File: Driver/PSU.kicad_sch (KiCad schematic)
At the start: 29 parts, among them J5 Jack-DC, U1 LM2596S-ADJ, U2 LM2674M-5.0, U3 LD1117S33TR

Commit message: 2
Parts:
- L2: footprint SamacSys_Parts:LQH43MN470K03L -> Inductor_SMD:L_1812_4532Metric_Pad1.30x3.40mm_HandSolder
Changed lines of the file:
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@@
 			)
 		)
-		(property "Footprint" "SamacSys_Parts:LQH43MN470K03L"
+		(property "Footprint" "Inductor_SMD:L_1812_4532Metric_Pad1.30x3.40mm_HandSolder"
 			(at 243.84 64.77 0)
 			(effects

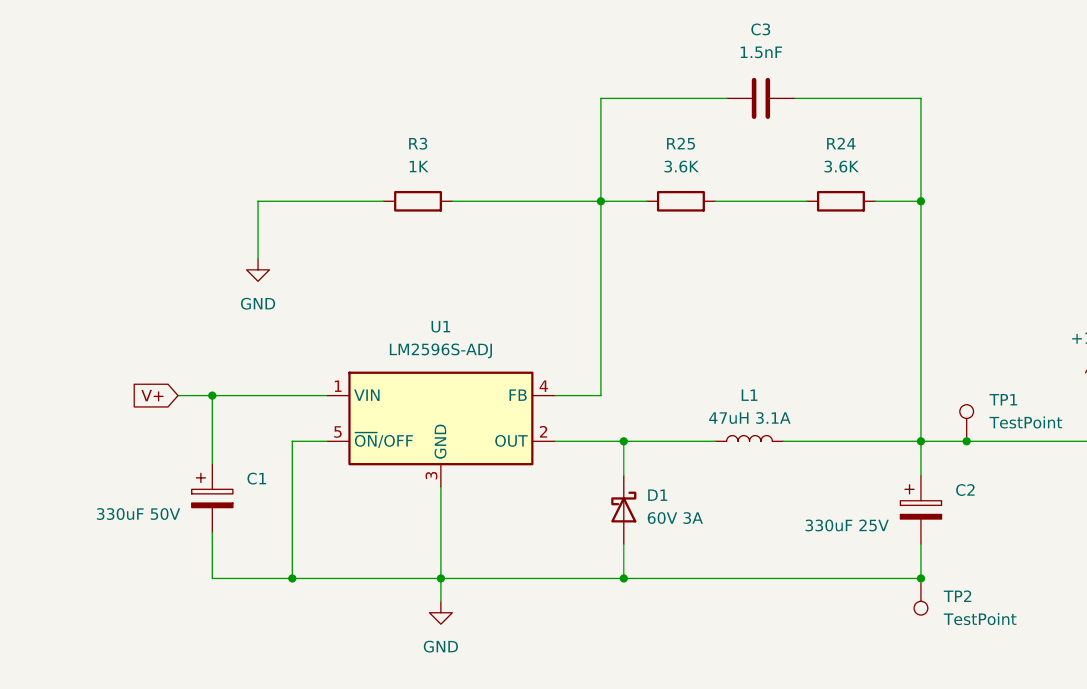
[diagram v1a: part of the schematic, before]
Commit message: Update a Connector and Trimpot
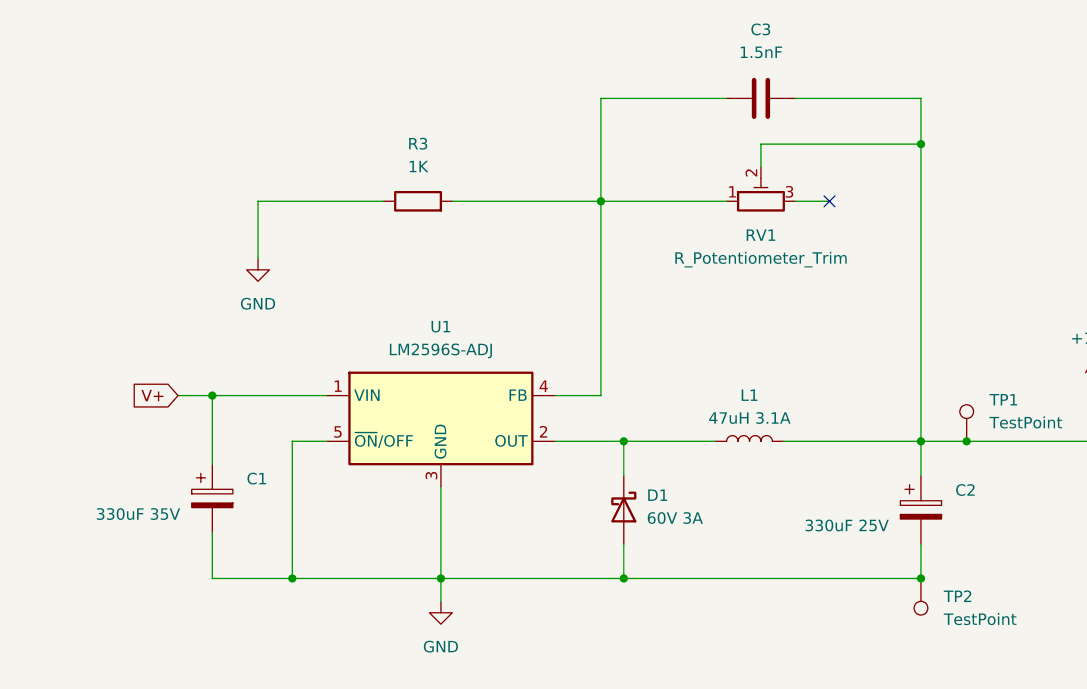
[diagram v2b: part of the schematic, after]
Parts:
- removed R24, R25: 3.6K, LED_SMD:LED_0805_2012Metric_Pad1.15x1.40mm_HandSolder, symbol Device:R
- added RV1: R_Potentiometer_Trim, Potentiometer_THT:Potentiometer_Bourns_3296W_Vertical, symbol Device:R_Potentiometer_Trim
- C1: value 330uF 50V -> 330uF 35V
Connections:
- net +10V: now also RV1.2
- net at C3.1, R3.2, U1.4 (FB): now also RV1.1
- no-connect marks 3 -> 4
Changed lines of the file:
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@@
-	)
-	(junction
-		(at 116.84 33.02)
-		(diameter 0)
-		(color 0 0 0 0)
 	)
 	(junction
@@
 	)
 	(junction
+		(at 116.84 26.67)
+		(diameter 0)
+		(color 0 0 0 0)
+	)
+	(junction
 		(at 241.3 54.61)
 		(diameter 0)
@@
 	)
 	(no_connect
+		(at 106.68 33.02)
+	)
+	(no_connect
 		(at 191.77 59.69)
 	)
@@
 	(wire
 		(pts
-			(xy 93.98 33.02) (xy 104.14 33.02)
-		)
-		(stroke
-			(width 0)
-			(type default)
-		)
-	)
-	(wire
-		(pts
 			(xy 38.1 74.93) (xy 46.99 74.93)
 		)
@@
 	(wire
 		(pts
-			(xy 81.28 33.02) (xy 86.36 33.02)
+			(xy 81.28 33.02) (xy 95.25 33.02)
 		)
 		(stroke
@@
 	(wire
 		(pts
+			(xy 102.87 33.02) (xy 106.68 33.02)
+		)
+		(stroke
+			(width 0)
+			(type default)
+		)
+	)
+	(wire
+		(pts
 			(xy 162.56 71.12) (xy 162.56 78.74)
 		)
@@
 	(wire
 		(pts
-			(xy 111.76 33.02) (xy 116.84 33.02)
-		)
-		(stroke
-			(width 0)
-			(type default)
-		)
-	)
-	(wire
-		(pts
 			(xy 201.93 119.38) (xy 214.63 119.38)
 		)
@@
 	(wire
 		(pts
-			(xy 116.84 21.59) (xy 116.84 33.02)
+			(xy 116.84 21.59) (xy 116.84 26.67)
 		)
 		(stroke
@@
 	(wire
 		(pts
-			(xy 116.84 33.02) (xy 116.84 59.69)
-		)
-		(stroke
-			(width 0)
-			(type default)
-		)
-	)
-	(wire
-		(pts
 			(xy 83.82 71.12) (xy 83.82 74.93)
 		)
@@
 	(wire
 		(pts
+			(xy 116.84 26.67) (xy 116.84 59.69)
+		)
+		(stroke
+			(width 0)
+			(type default)
+		)
+	)
+	(wire
+		(pts
 			(xy 172.72 119.38) (xy 172.72 123.19)
 		)
@@
 	(wire
 		(pts
+			(xy 99.06 26.67) (xy 116.84 26.67)
+		)
+		(stroke
+			(width 0)
+			(type default)
+		)
+	)
+	(wire
+		(pts
 			(xy 204.47 80.01) (xy 204.47 78.74)
 		)
@@
 		(pts
 			(xy 64.77 33.02) (xy 81.28 33.02)
+		)
+		(stroke
+			(width 0)
+			(type default)
+		)
+	)
+	(wire
+		(pts
+			(xy 99.06 26.67) (xy 99.06 29.21)
 		)
 		(stroke
@@
 	)
 	(symbol
-		(lib_id "Device:R")
-		(at 107.95 33.02 90)
-		(unit 1)
-		(exclude_from_sim no)
-		(in_bom yes)
-		(on_board yes)
-		(dnp no)
-		(fields_autoplaced yes)
-		(property "Reference" "R24"
-			(at 107.95 26.67 90)
-			(effects
-				(font
-					(size 1.27 1.27)
-				)
-			)
-		)
-		(property "Value" "3.6K"
-			(at 107.95 29.21 90)
-			(effects
-				(font
-					(size 1.27 1.27)
-				)
-			)
-		)
-		(property "Footprint" "LED_SMD:LED_0805_2012Metric_Pad1.15x1.40mm_HandSolder"
-			(at 107.95 34.798 90)
-			(effects
-				(font
-					(size 1.27 1.27)
-				)
-				(hide yes)
-			)
-		)
-		(property "Datasheet" "~"
-			(at 107.95 33.02 0)
-			(effects
-				(font
-					(size 1.27 1.27)
-				)
-				(hide yes)
-			)
-		)
-		(property "Description" "Resistor"
-			(at 107.95 33.02 0)
-			(effects
-				(font
-					(size 1.27 1.27)
-				)
-				(hide yes)
-			)
-		)
-		(pin "1"
-		)
-		(pin "2"
-		)
-		(instances
-			(project "Driver"
-				(path "/ea1eaa3d-8f21-4909-90ab-d62ac3efaefb/fbf7fa7d-f118-4c25-bcc8-4a06edb726c3"
-					(reference "R24")
-					(unit 1)
-				)
-			)
-		)
-	)
-	(symbol
 		(lib_id "SamacSys_Parts:XT60PW-M")
 		(at 25.4 99.06 0)
@@
 			)
 		)
-		(property "Value" "330uF 50V"
+		(property "Value" "330uF 35V"
 			(at 25.146 67.818 0)
 			(effects
@@
 	)
 	(symbol
-		(lib_id "Device:R")
-		(at 90.17 33.02 90)
-		(unit 1)
-		(exclude_from_sim no)
-		(in_bom yes)
-		(on_board yes)
-		(dnp no)
-		(fields_autoplaced yes)
-		(property "Reference" "R25"
-			(at 90.17 26.67 90)
-			(effects
-				(font
-					(size 1.27 1.27)
-				)
-			)
-		)
-		(property "Value" "3.6K"
-			(at 90.17 29.21 90)
-			(effects
-				(font
-					(size 1.27 1.27)
-				)
-			)
-		)
-		(property "Footprint" "LED_SMD:LED_0805_2012Metric_Pad1.15x1.40mm_HandSolder"
-			(at 90.17 34.798 90)
-			(effects
-				(font
-					(size 1.27 1.27)
-				)
-				(hide yes)
-			)
-		)
-		(property "Datasheet" "~"
-			(at 90.17 33.02 0)
-			(effects
-				(font
-					(size 1.27 1.27)
-				)
-				(hide yes)
-			)
-		)
-		(property "Description" "Resistor"
-			(at 90.17 33.02 0)
-			(effects
-				(font
-					(size 1.27 1.27)
-				)
-				(hide yes)
-			)
-		)
-		(pin "1"
-		)
-		(pin "2"
-		)
-		(instances
-			(project "Driver"
-				(path "/ea1eaa3d-8f21-4909-90ab-d62ac3efaefb/fbf7fa7d-f118-4c25-bcc8-4a06edb726c3"
-					(reference "R25")
-					(unit 1)
-				)
-			)
-		)
-	)
-	(symbol
 		(lib_id "Connector:TestPoint")
 		(at 116.84 74.93 180)
@@
 					(unit 1)
 				)
+			)
+		)
+	)
+	(symbol
+		(lib_id "Device:R_Potentiometer_Trim")
+		(at 99.06 33.02 90)
+		(unit 1)
+		(exclude_from_sim no)
+		(in_bom yes)
+		(on_board yes)
+		(dnp no)
+		(fields_autoplaced yes)
+		(property "Reference" "RV1"
+			(at 99.06 36.83 90)
+			(effects
+				(font
+					(size 1.27 1.27)
+				)
+			)
+		)
+		(property "Value" "R_Potentiometer_Trim"
+			(at 99.06 39.37 90)
+			(effects
+				(font
+					(size 1.27 1.27)
+				)
+			)
+		)
+		(property "Footprint" "Potentiometer_THT:Potentiometer_Bourns_3296W_Vertical"
+			(at 99.06 33.02 0)
+			(effects
+				(font
+					(size 1.27 1.27)
+				)
+				(hide yes)
+			)
+		)
+		(property "Datasheet" "~"
+			(at 99.06 33.02 0)
+			(effects
+				(font
+					(size 1.27 1.27)
+				)
+				(hide yes)
+			)
+		)
+		(property "Description" "Trim-potentiometer"
+			(at 99.06 33.02 0)
+			(effects
+				(font
+					(size 1.27 1.27)
+				)
+				(hide yes)
+			)
+		)
+		(pin "2"
+		)
+		(pin "1"
+		)
+		(pin "3"
+		)
+		(instances
+			(project ""
+				(path "/ea1eaa3d-8f21-4909-90ab-d62ac3efaefb/fbf7fa7d-f118-4c25-bcc8-4a06edb726c3"
+					(reference "RV1")
+					(unit 1)
+				)
